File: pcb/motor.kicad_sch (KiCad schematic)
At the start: 4 parts, among them J11 Conn_01x02_Pin, U8 DRV8837

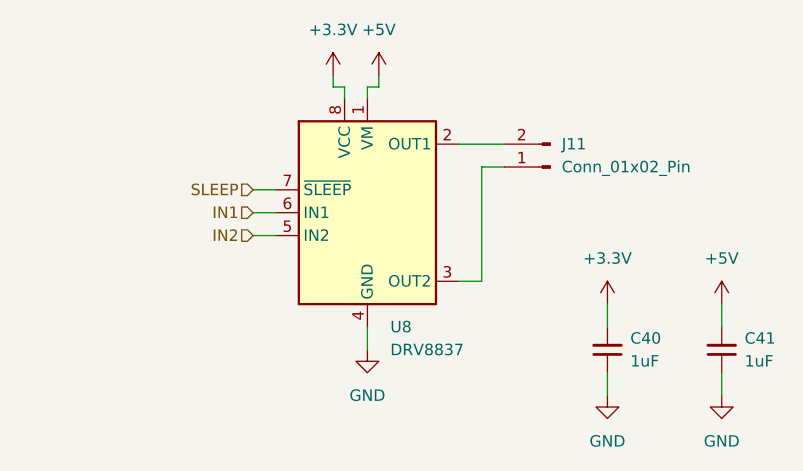
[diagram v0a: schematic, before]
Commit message: fixes #10
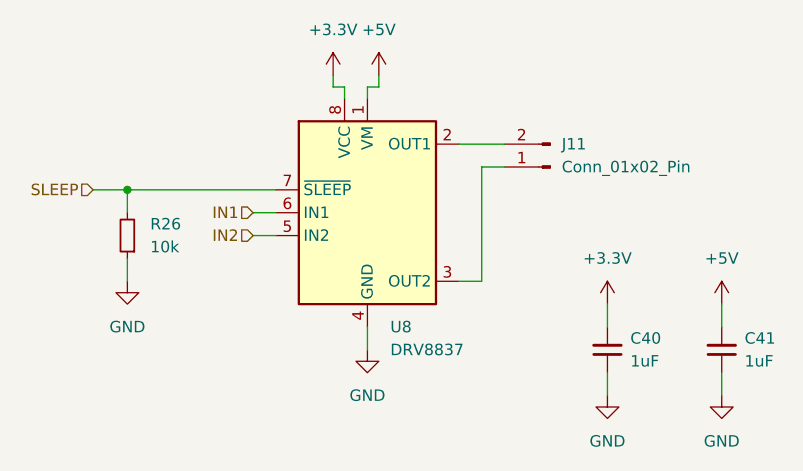
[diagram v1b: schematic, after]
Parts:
- added R26: 10k, Resistor_SMD:R_0603_1608Metric, symbol Device:R_Small
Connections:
- net GND: now also R26.1
- net SLEEP: now also R26.2
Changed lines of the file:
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@@
 	(generator_version "9.0")
 	(paper "A4")
+	(junction
+		(at 107.95 88.9)
+		(diameter 0)
+		(color 0 0 0 0)
+	)
+	(wire
+		(pts
+			(xy 107.95 88.9) (xy 107.95 91.44)
+		)
+		(stroke
+			(width 0)
+			(type default)
+		)
+	)
 	(wire
 		(pts
@@
 	(wire
 		(pts
-			(xy 121.92 88.9) (xy 124.46 88.9)
+			(xy 104.14 88.9) (xy 107.95 88.9)
 		)
 		(stroke
@@
 	(wire
 		(pts
+			(xy 107.95 96.52) (xy 107.95 99.06)
+		)
+		(stroke
+			(width 0)
+			(type default)
+		)
+	)
+	(wire
+		(pts
 			(xy 144.78 99.06) (xy 147.32 99.06)
 		)
@@
 		(pts
 			(xy 173.99 101.6) (xy 173.99 104.14)
+		)
+		(stroke
+			(width 0)
+			(type default)
+		)
+	)
+	(wire
+		(pts
+			(xy 107.95 88.9) (xy 124.46 88.9)
 		)
 		(stroke
@@
 	(hierarchical_label "SLEEP"
 		(shape input)
-		(at 121.92 88.9 180)
+		(at 104.14 88.9 180)
 		(effects
 			(font
@@
 	)
 	(symbol
+		(lib_id "Device:R_Small")
+		(at 107.95 93.98 180)
+		(unit 1)
+		(exclude_from_sim no)
+		(in_bom yes)
+		(on_board yes)
+		(dnp no)
+		(fields_autoplaced yes)
+		(property "Reference" "R26"
+			(at 110.49 92.7099 0)
+			(effects
+				(font
+					(size 1.27 1.27)
+				)
+				(justify right)
+			)
+		)
+		(property "Value" "10k"
+			(at 110.49 95.2499 0)
+			(effects
+				(font
+					(size 1.27 1.27)
+				)
+				(justify right)
+			)
+		)
+		(property "Footprint" "Resistor_SMD:R_0603_1608Metric"
+			(at 107.95 93.98 0)
+			(effects
+				(font
+					(size 1.27 1.27)
+				)
+				(hide yes)
+			)
+		)
+		(property "Datasheet" "~"
+			(at 107.95 93.98 0)
+			(effects
+				(font
+					(size 1.27 1.27)
+				)
+				(hide yes)
+			)
+		)
+		(property "Description" "Resistor, small symbol"
+			(at 107.95 93.98 0)
+			(effects
+				(font
+					(size 1.27 1.27)
+				)
+				(hide yes)
+			)
+		)
+		(pin "1"
+		)
+		(pin "2"
+		)
+		(instances
+			(project "longboi"
+				(path "/0a1f9f3d-7c96-45bd-a844-76a0eed80de7/2af30998-db5e-4628-a14e-5eba2e825222"
+					(reference "R27")
+					(unit 1)
+				)
+				(path "/0a1f9f3d-7c96-45bd-a844-76a0eed80de7/3a33a4cf-cd5c-42b4-b4f4-be366a1e5be4"
+					(reference "R68")
+					(unit 1)
+				)
+				(path "/0a1f9f3d-7c96-45bd-a844-76a0eed80de7/516d94da-e85f-4db4-853b-114c3e517177"
+					(reference "R67")
+					(unit 1)
+				)
+				(path "/0a1f9f3d-7c96-45bd-a844-76a0eed80de7/d37b1df8-e268-4063-94df-2485b04b54f8"
+					(reference "R26")
+					(unit 1)
+				)
+			)
+		)
+	)
+	(symbol
 		(lib_id "power:+3.3V")
 		(at 161.29 101.6 0)
@@
 					(unit 1)
 				)
+			)
+		)
+	)
+	(symbol
+		(lib_id "power:GND")
+		(at 107.95 99.06 0)
+		(unit 1)
+		(exclude_from_sim no)
+		(in_bom yes)
+		(on_board yes)
+		(dnp no)
+		(fields_autoplaced yes)
+		(property "Reference" "#PWR0214"
+			(at 107.95 105.41 0)
+			(effects
+				(font
+					(size 1.27 1.27)
+				)
+				(hide yes)
+			)
+		)
+		(property "Value" "GND"
+			(at 107.95 104.14 0)
+			(effects
+				(font
+					(size 1.27 1.27)
+				)
+			)
+		)
+		(property "Footprint" ""
+			(at 107.95 99.06 0)
+			(effects
+				(font
+					(size 1.27 1.27)
+				)
+				(hide yes)
+			)
+		)
+		(property "Datasheet" ""
+			(at 107.95 99.06 0)
+			(effects
+				(font
+					(size 1.27 1.27)
+				)
+				(hide yes)
+			)
+		)
+		(property "Description" "Power symbol creates a global label with name \"GND\" , ground"
+			(at 107.95 99.06 0)
+			(effects
+				(font
+					(size 1.27 1.27)
+				)
+				(hide yes)
+			)
+		)
+		(pin "1"
+		)
+		(instances
+			(project "longboi"
+				(path "/0a1f9f3d-7c96-45bd-a844-76a0eed80de7/2af30998-db5e-4628-a14e-5eba2e825222"
+					(reference "#PWR0215")
+					(unit 1)
+				)
+				(path "/0a1f9f3d-7c96-45bd-a844-76a0eed80de7/3a33a4cf-cd5c-42b4-b4f4-be366a1e5be4"
+					(reference "#PWR0218")
+					(unit 1)
+				)
+				(path "/0a1f9f3d-7c96-45bd-a844-76a0eed80de7/516d94da-e85f-4db4-853b-114c3e517177"
+					(reference "#PWR0217")
+					(unit 1)
+				)
+				(path "/0a1f9f3d-7c96-45bd-a844-76a0eed80de7/d37b1df8-e268-4063-94df-2485b04b54f8"
+					(reference "#PWR0214")
+					(unit 1)
+				)

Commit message: specified some values and colors added lcsc part ids for all components
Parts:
- C40, C41: LCSC (none) -> C15849
- J11: LCSC (none) -> C378939
- R26: LCSC (none) -> C98220
- U8: LCSC (none) -> C39159
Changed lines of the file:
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@@
+			)
+		)
+		(property "LCSC" "C98220"
+			(at 110.49 92.7099 0)
+			(effects
+				(font
+					(size 1.27 1.27)
+				)
+				(hide yes)
 			)
 		)
@@
 			)
 		)
+		(property "LCSC" "C378939"
+			(at 156.21 83.82 0)
+			(effects
+				(font
+					(size 1.27 1.27)
+				)
+				(hide yes)
+			)
+		)
 		(pin "1"
 		)
@@
 			)
 		)
+		(property "LCSC" "C15849"
+			(at 163.83 105.4036 0)
+			(effects
+				(font
+					(size 1.27 1.27)
+				)
+				(hide yes)
+			)
+		)
 		(pin "2"
 		)
@@
 			)
 		)
+		(property "LCSC" "C39159"
+			(at 137.1618 104.14 0)
+			(effects
+				(font
+					(size 1.27 1.27)
+				)
+				(hide yes)
+			)
+		)
 		(pin "6"
 		)
@@
 			(effects
 				(font
+					(size 1.27 1.27)
+				)
+				(hide yes)
+			)
+		)
+		(property "LCSC" "C15849"
+			(at 176.53 105.4036 0)
+			(effects
+				(font
